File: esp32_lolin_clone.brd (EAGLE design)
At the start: 25 x 58 mm, 33 parts, among them J1 10104111-0001LF, P1 S2B-PH-SM4-TB, Q1 CJ2301S1, Q2 CJ2301S1, SW1 PTS815SJK250SMTR, U1 ESP32-WROOM-32D, U2 BCM857, U3 ME6211, U4 UMH3N, U5 TP4054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

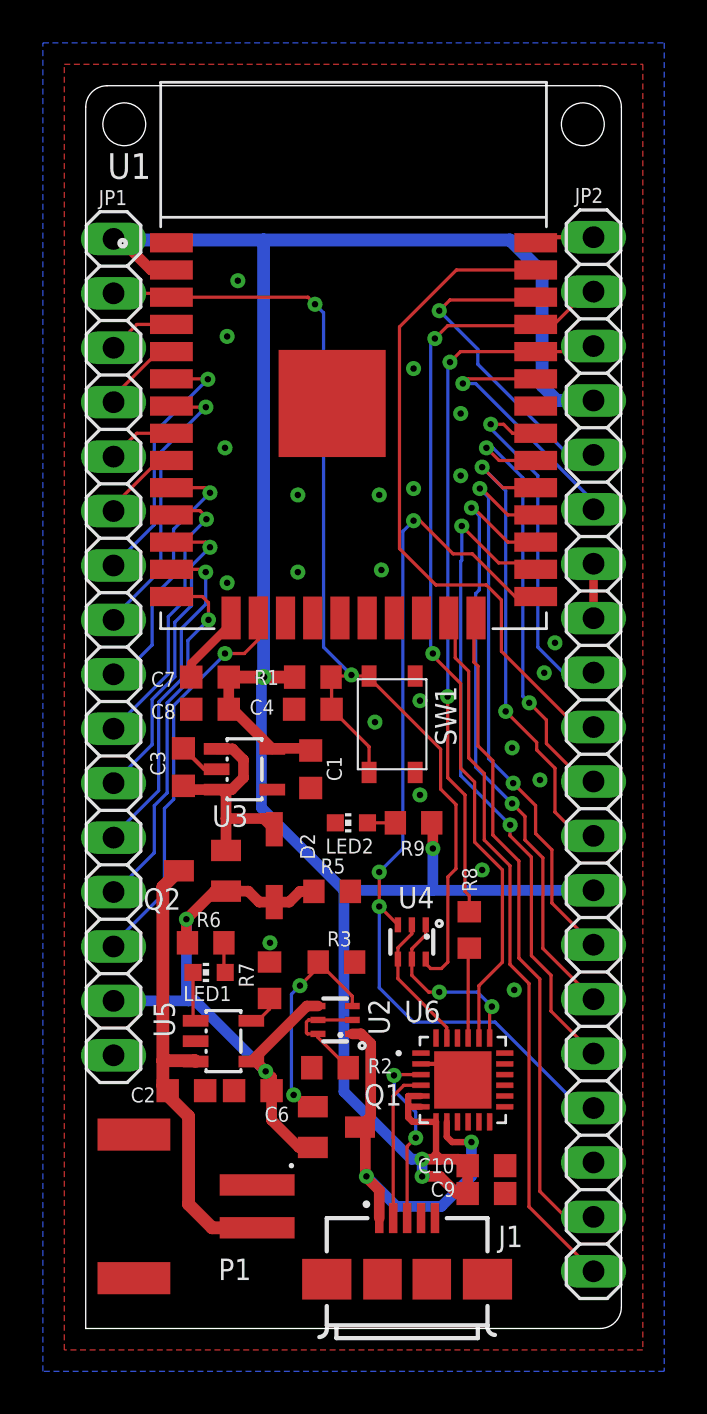
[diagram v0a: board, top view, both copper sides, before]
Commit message: - Change device reference BCM857, so it really matches the footprint at the board.
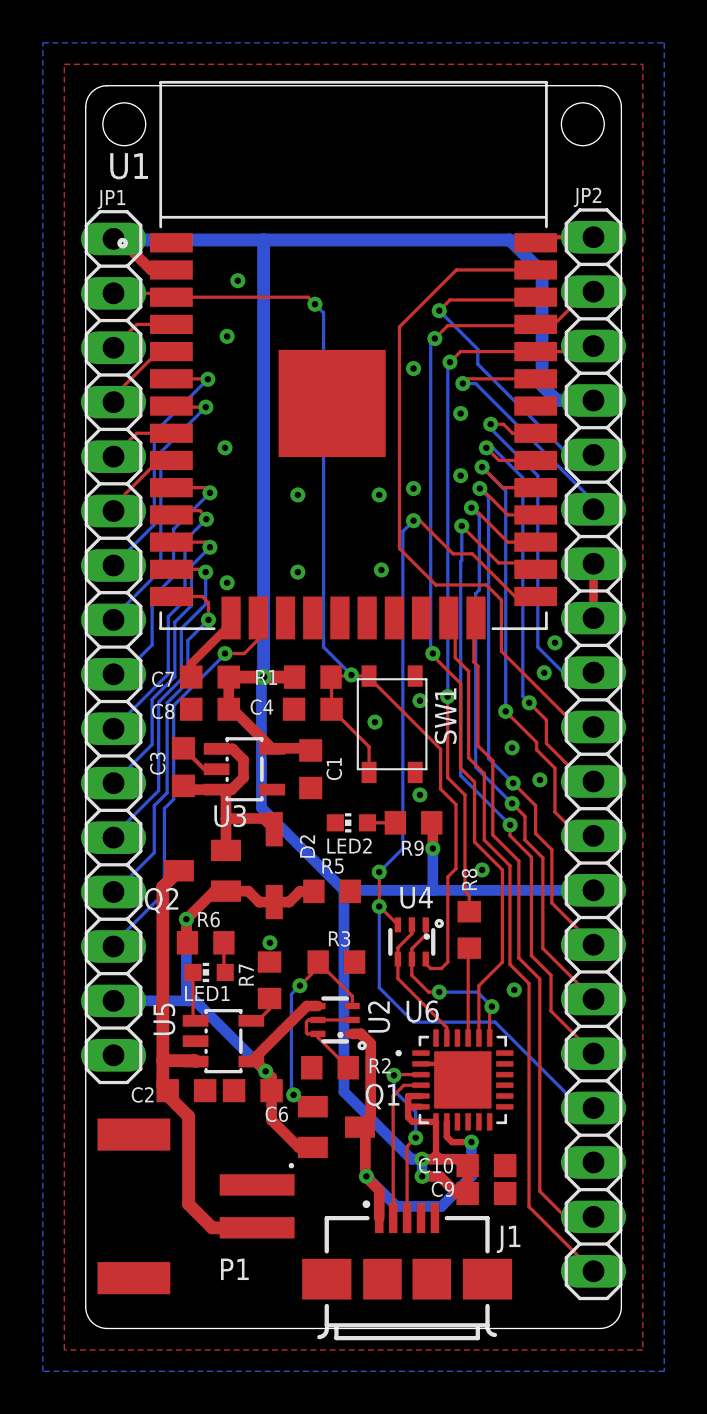
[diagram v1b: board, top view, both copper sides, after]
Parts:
- added U$1: (no value), RE_common:RE_LOGO_10MM
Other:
- outline, holes or cut-outs redrawn
- board text added: ">DRAWING_NAME"
- board text added: ">PLOT_DATE_TIME"
- board text added: "Raul Quesada"
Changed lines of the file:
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@@
 <drawing>
 <settings>
-<setting alwaysvectorfont="yes"/>
+<setting alwaysvectorfont="no"/>
 <setting verticaltext="up"/>
 </settings>
-<grid distance="0.1" unitdist="mm" unit="mm" style="lines" multiple="1" display="yes" altdistance="5" altunitdist="mil" altunit="mil"/>
+<grid distance="1" unitdist="mm" unit="mm" style="lines" multiple="1" display="yes" altdistance="5" altunitdist="mil" altunit="mil"/>
 <layers>
 <layer number="1" name="Top" color="4" fill="1" visible="yes" active="yes"/>
@@
 <wire x1="24" y1="58" x2="1" y2="58" width="0" layer="20"/>
 <wire x1="1" y1="58" x2="0" y2="57" width="0" layer="20" curve="90"/>
-<wire x1="0" y1="57" x2="0" y2="0" width="0" layer="20"/>
-<wire x1="0" y1="0" x2="24" y2="0" width="0" layer="20"/>
+<wire x1="0" y1="57" x2="0" y2="1" width="0" layer="20"/>
+<wire x1="0" y1="1" x2="1" y2="0" width="0" layer="20" curve="90"/>
+<wire x1="1" y1="0" x2="24" y2="0" width="0" layer="20"/>
 <wire x1="24" y1="0" x2="25" y2="1" width="0" layer="20" curve="90"/>
 <wire x1="25" y1="1" x2="25" y2="57" width="0" layer="20"/>
@@
 <circle x="12.9" y="13.2" radius="0.14141875" width="0.1524" layer="21"/>
 <circle x="16.5" y="18.9" radius="0.14141875" width="0.1524" layer="21"/>
+<text x="8.75" y="16.75" size="1" layer="26" font="vector" ratio="15" rot="MR90">Raul Quesada</text>
+<text x="6.85" y="16.65" size="1" layer="26" font="vector" ratio="15" rot="MR90">&gt;PLOT_DATE_TIME</text>
+<text x="10.55" y="16.65" size="1" layer="26" font="vector" ratio="15" rot="MR90">&gt;DRAWING_NAME</text>
 </plain>
 <attributes>
@@
 <element name="U2" library="RE_wemos_lolin_clone" package="SOT363_INFINEON" value="BCM857" x="11.64" y="14.4" smashed="yes" rot="R90">
 <attribute name="DISTRIBUTOR" value="Mouser" x="47.2" y="39.8" size="1.778" layer="27" rot="R90" display="off"/>
-<attribute name="DISTRIBUTOR_REF" value="771-BCM857DS135" x="47.2" y="39.8" size="1.778" layer="27" rot="R90" display="off"/>
+<attribute name="DISTRIBUTOR_REF" value="771-BCM857BS135" x="47.2" y="39.8" size="1.778" layer="27" rot="R90" display="off"/>
 <attribute name="MANUFACTURER" value="Nexperia" x="47.2" y="39.8" size="1.778" layer="27" rot="R90" display="off"/>
-<attribute name="MANUFACTURER_REF" value="BCM857DS,135" x="47.2" y="39.8" size="1.778" layer="27" rot="R90" display="off"/>
+<attribute name="MANUFACTURER_REF" value="BCM857BS,135" x="47.2" y="39.8" size="1.778" layer="27" rot="R90" display="off"/>
 <attribute name="NAME" x="14.19" y="13.7" size="1" layer="25" font="vector" ratio="15" rot="R90"/>
 <attribute name="VALUE" x="14.34" y="13.3" size="1.27" layer="27" rot="R90"/>
@@
 <attribute name="VALUE" x="3.9" y="9.45" size="1.016" layer="27"/>
 </element>
+<element name="U$1" library="RE_common" package="RE_LOGO_10MM" value="" x="7.6894" y="9.1592" smashed="yes" rot="MR90"/>
 </elements>
 <signals>

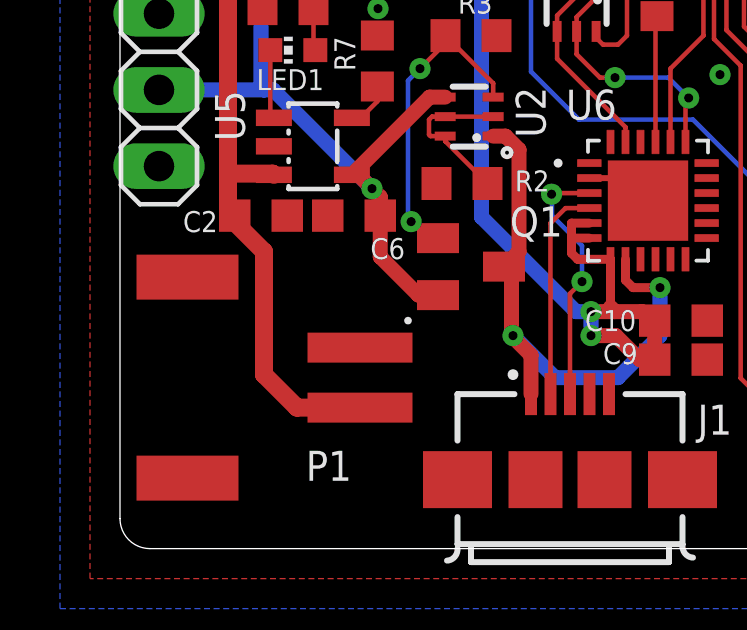
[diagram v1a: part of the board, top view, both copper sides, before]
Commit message: - FIX CRITICAL ERROR: Battery connector pins were swapped.
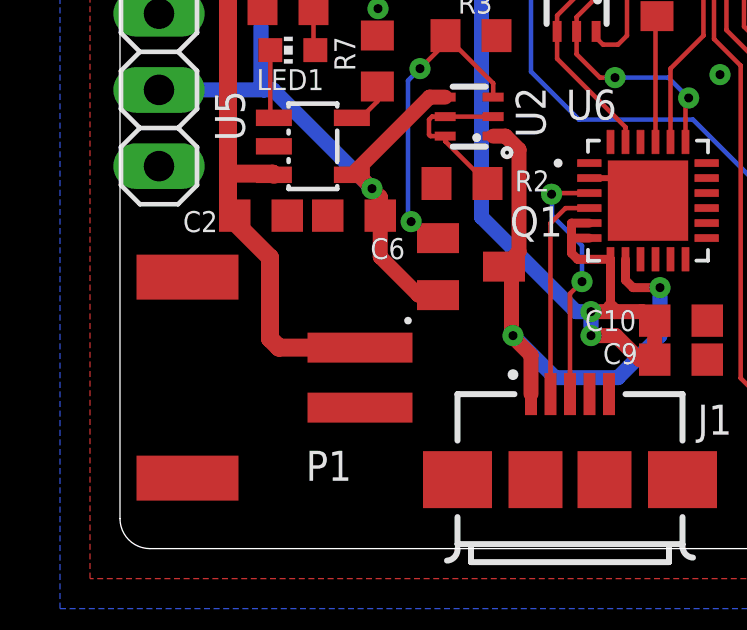
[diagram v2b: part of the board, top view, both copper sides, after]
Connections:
- net GND: now also P1.2; no longer P1.1
- net VBAT: now also P1.1; no longer P1.2
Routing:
- net VBAT: track 21.6 -> 19.9 mm
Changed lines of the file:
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@@
 <contactref element="C6" pad="2"/>
 <contactref element="R7" pad="2"/>
-<contactref element="P1" pad="1"/>
 <contactref element="C9" pad="2"/>
 <contactref element="C10" pad="2"/>
@@
 <via x="15.6" y="29.3" extent="1-16" drill="0.3"/>
 <via x="13.5" y="28.3" extent="1-16" drill="0.3"/>
+<contactref element="P1" pad="2"/>
 </signal>
 <signal name="N$1">
@@
 <contactref element="Q2" pad="3"/>
 <contactref element="U5" pad="3"/>
-<contactref element="P1" pad="2"/>
 <contactref element="C2" pad="1"/>
-<wire x1="8" y1="4.7" x2="5.9" y2="4.7" width="0.6" layer="1"/>
 <wire x1="3.825" y1="10.875" x2="3.825" y2="11.1" width="0.6" layer="1"/>
-<wire x1="5.9" y1="4.7" x2="4.8" y2="5.8" width="0.6" layer="1"/>
-<wire x1="4.8" y1="5.8" x2="4.8" y2="9.9" width="0.6" layer="1"/>
-<wire x1="4.8" y1="9.9" x2="3.825" y2="10.875" width="0.6" layer="1"/>
 <wire x1="3.825" y1="11.1" x2="3.6" y2="11.325" width="0.6" layer="1"/>
 <wire x1="3.6" y1="20.611" x2="4.349" y2="21.36" width="0.6" layer="1"/>
@@
 <wire x1="5.1299" y1="12.46" x2="5.0899" y2="12.5" width="0.6" layer="1"/>
 <wire x1="5.0899" y1="12.5" x2="3.6" y2="12.5" width="0.6" layer="1"/>
+<contactref element="P1" pad="1"/>
+<wire x1="8" y1="6.7" x2="5.3" y2="6.7" width="0.6" layer="1"/>
+<wire x1="5.3" y1="6.7" x2="5" y2="7" width="0.6" layer="1"/>
+<wire x1="5" y1="7" x2="5" y2="9.7" width="0.6" layer="1"/>
+<wire x1="5" y1="9.7" x2="3.825" y2="10.875" width="0.6" layer="1"/>
 </signal>
 <signal name="N$9">
